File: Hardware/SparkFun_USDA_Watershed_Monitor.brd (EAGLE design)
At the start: 63.5 x 63.5 mm, 194 parts, among them J10 QWIIC_RIGHT_ANGLE, J3 QWIIC_RIGHT_ANGLE, J4 U.FL, J5 RJ45, J7 RJ45, J9 RJ45, Q1 20V/4.2A/52mΩ/1.4W, Q2 20V/0.2A/8MHz/1.2Ω/1Vth, Q3 20V/0.2A/8MHz/1.2Ω/1Vth, Q4 20V/0.2A/8MHz/1.2Ω/1Vth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

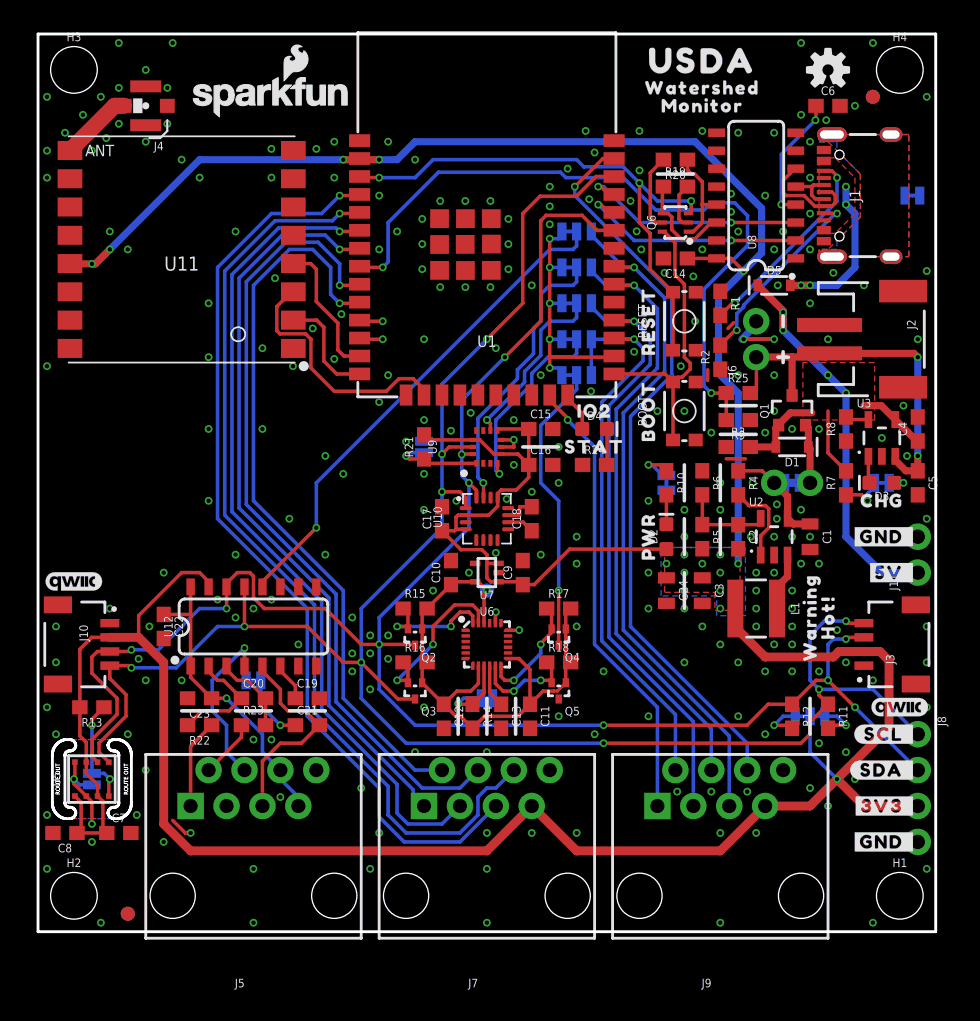
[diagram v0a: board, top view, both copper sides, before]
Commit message: Connect RFM95W pins
Somebody forgot to connect them...
Connect ESP32's IO5 and IO15 (both internally pulled high) to RFM's RESET and CS respectively
Connect ESP32's IO26 and IO27 to RFM's IO1 and IO0 respectively (IO2 not needed for LoRa)
ESP32's IO15, IO26, and IO27 are no longer broken out to RJ45 or headers
Add pullup resistor to ESP_EN
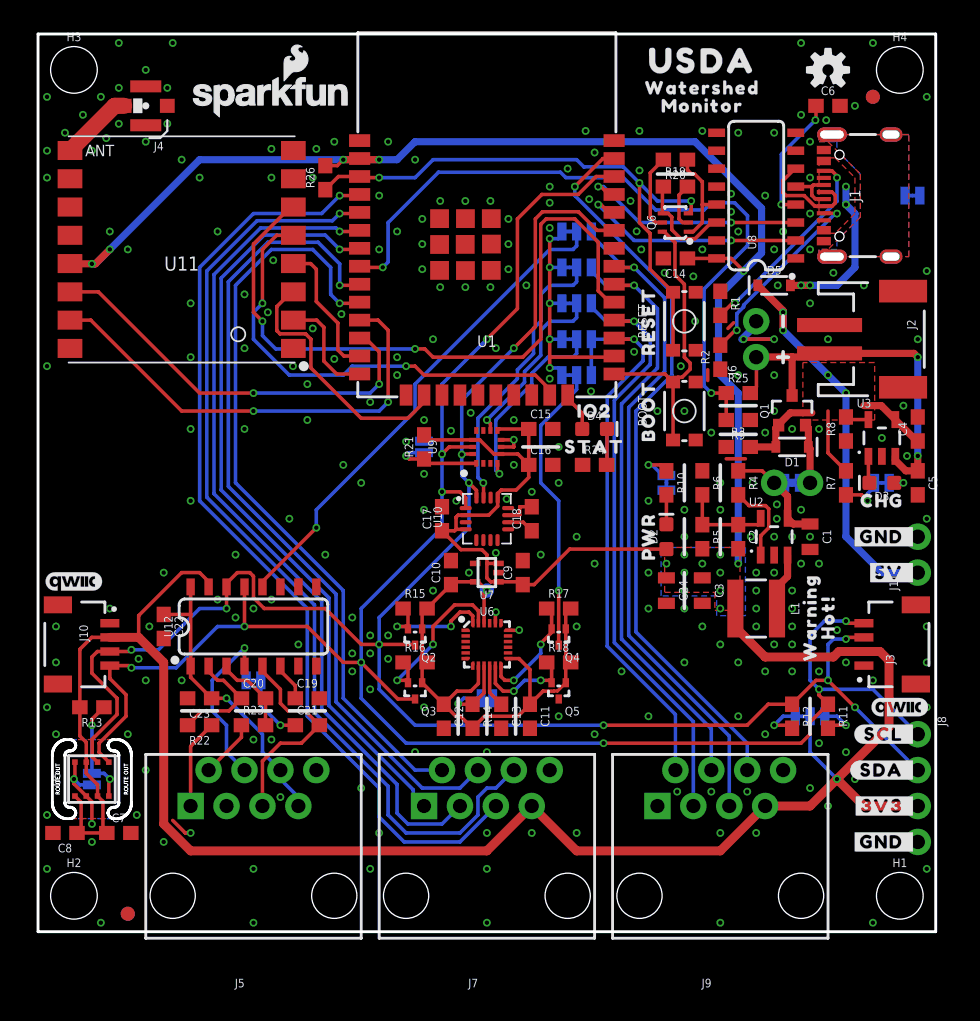
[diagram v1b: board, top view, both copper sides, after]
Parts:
- removed U$55: (no value), output:IO150
- added R26: 100k, SparkFun-Resistors:0603
- added U$49: (no value), output:NC0
- moved U$54 57.0 mm to (29.8, 3.05)
- moved U$63 54.0 mm to (33.7, 3.05)
- moved U$64 53.7 mm to (29.8, 4.57)
- moved U$61 53.3 mm to (33.7, 4.57)
- moved U$52 53.0 mm to (29.8, 6.10)
- moved U$62 49.0 mm to (33.7, 6.10)
- moved U$32 37.9 mm to (50.2, 18.8)
- moved U$33 37.9 mm to (46.4, 18.8)
- moved U$34 37.9 mm to (50.2, 17.3)
- moved U$35 37.9 mm to (46.4, 17.3)
- moved U$36 37.9 mm to (50.2, 15.7)
- moved U$37 37.9 mm to (46.4, 15.7)
- moved U$38 37.9 mm to (50.2, 14.2)
- moved U$39 37.9 mm to (46.4, 14.2)
- moved U$45 37.9 mm to (48.3, 20.3)
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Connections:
- removed net ESP_IO15: J9.1, U1.23
- removed net ESP_IO26: U1.11
- removed net ESP_IO27: U1.12
- removed net ESP_IO5: U1.29
- removed net IO26: U11.NSS
- removed net IO27: U11.DIO2
- removed net IO32: U11.DIO1
- removed net IO33: U11.DIO0
- new net !RFM_CS!: U1.23, U11.NSS
- new net RFM_IO0: U1.12, U11.DIO0
- new net RFM_IO1: U1.11, U11.DIO1
- net !RFM_RST!: now also U1.29
- net 3.3V: now also R26.2
- net ESP_EN: now also R26.1
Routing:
- net !RFM_RST!: track 0.00 -> 49.4 mm, vias 0 -> 2
- net RFM_IO1: track 0.00 -> 32.8 mm, vias 0 -> 2
- net !RFM_CS!: track 0.00 -> 32.6 mm, vias 0 -> 2
- net ESP_IO15: track 32.2 -> 0.00 mm, vias 1 -> 0
- net RFM_IO0: track 0.00 -> 29.2 mm, vias 0 -> 2
- net ESP_EN: track 39.0 -> 41.8 mm
- net ESP_IO33: track 56.8 -> 58.6 mm
- net ESP_I36: track 65.8 -> 67.6 mm
- net ESP_I34: track 58.8 -> 60.6 mm
- net ESP_IO25: track 52.2 -> 54.0 mm
- net ESP_I35: track 53.0 -> 54.8 mm
- net ESP_I39: track 66.5 -> 68.3 mm
- net ESP_IO27: track 1.67 -> 0.00 mm, vias 1 -> 0
- net ESP_IO26: track 1.67 -> 0.00 mm, vias 1 -> 0
- net 3.3V: track 267.7 -> 269.1 mm
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
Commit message: Design review updates
Remove 3V3_EN and ICM's FSYNC nets (won't be used)
Add diode to NAU_INT (chip doesn't do open-drain)
Clarify interrupts needing to be open-drain, active high
Fix ICM interrupt level shifter output to be high-Z when input is low (or high-Z), and drive high when input is high
Add version number to copper
Add silk labels to RJ45s, and dashed lines connecting pinout to color code
Add IMU axis albels to silk
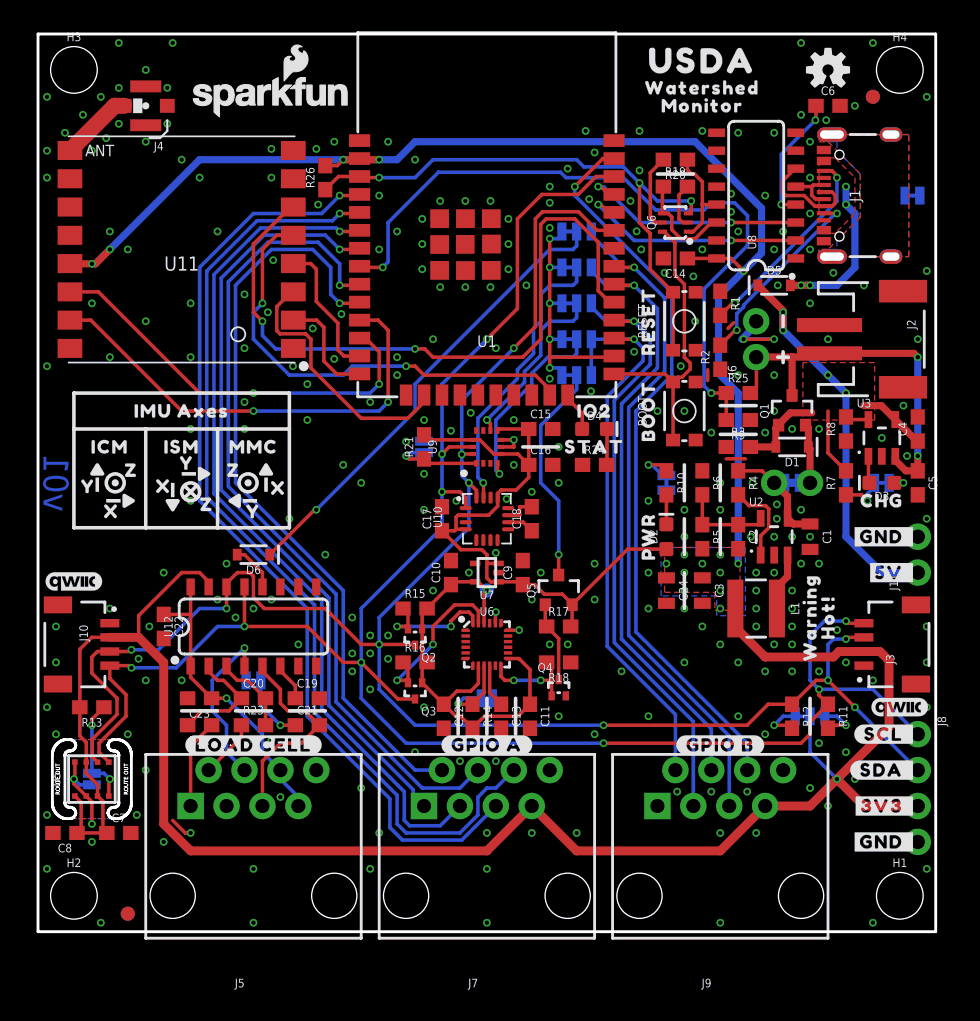
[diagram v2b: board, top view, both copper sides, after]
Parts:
- added D6: 3A/10V/280mV, SparkFun-DiscreteSemi:SOD-323
- added U$100, U$104, U$107, U$88, U$91, U$94: (no value), output:X0
- added U$101, U$113: (no value), output:IMU_AXES0
- added U$102, U$105, U$108, U$89, U$92, U$95: (no value), output:Y0
- added U$103, U$106, U$109, U$90, U$93, U$96: (no value), output:Z0
- added U$110, U$97: (no value), output:ICM0
- added U$111, U$98: (no value), output:ISM0
- added U$112, U$99: (no value), output:MMC0
- added U$50, U$55: (no value), output:#LOAD_CELL#0
- added U$51, U$86: (no value), output:#GPIO_A#0
- added U$53, U$87: (no value), output:#GPIO_B#0
- Q5: value 20V/0.2A/8MHz/1.2Ω/1Vth -> 20V/4.2A/52mΩ/1.4W; device SparkFun-DiscreteSemi:SOT-416FL -> SparkFun-DiscreteSemi:SOT23-3
- R17, R18: value 2.2k -> 100k
- moved Q5 7.62 mm to (36.8, 24.1), turned to 0 degrees
- moved Q4 2.54 mm to (36.8, 17.8), turned to 0 degrees
- moved R17 1.27 mm to (36.8, 21.6)
- moved U$12 0.38 mm to (17.1, 5.71)
- moved U$40 0.38 mm to (13.3, 5.71)
- moved U$41 0.38 mm to (17.1, 2.67)
- moved U$42 0.38 mm to (13.3, 2.67)
- moved U$43 0.38 mm to (17.1, 4.19)
- moved U$44 0.38 mm to (13.3, 4.19)
- moved U$49 0.38 mm to (50.2, 5.71)
- moved U$52 0.38 mm to (29.8, 5.71)
- moved U$54 0.38 mm to (29.8, 2.67)
- moved U$57 0.38 mm to (46.4, 5.71)
- moved U$58 0.38 mm to (50.2, 4.19)
- moved U$59 0.38 mm to (46.4, 2.67)
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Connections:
- removed net ICM_FSYNC: Q5.3
- removed net ICM_FSYNC_1V8: Q5.2, R18.1, U6.11
- new net N$29: D6.A, U12.12
- new net N$30: Q4.3, Q5.1, R17.1
- net 1.8V: no longer Q4.1, Q5.1, R17.2, R18.2
- net 3.3V: now also Q5.2, R17.2
- net GND: now also Q4.2, R18.1
- net ICM_INT: now also Q5.3; no longer Q4.3
- net ICM_INT_1V8: now also Q4.1, R18.2; no longer Q4.2, R17.1
- net NAU_INT: now also D6.C; no longer U12.12
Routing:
- net 1.8V: track 40.4 -> 31.6 mm
- net ICM_FSYNC_1V8: track 7.43 -> 0.00 mm, vias 2 -> 0
- net N$30: track 0.00 -> 5.69 mm
- net ICM_INT: track 20.7 -> 15.7 mm
- net N$29: track 0.00 -> 3.32 mm
- net 3.3V: track 269.1 -> 271.9 mm
- net NAU_INT: track 35.3 -> 32.9 mm
- net ICM_INT_1V8: track 8.07 -> 6.92 mm
- net GND: vias 264 -> 271
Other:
- board text added: "v01"

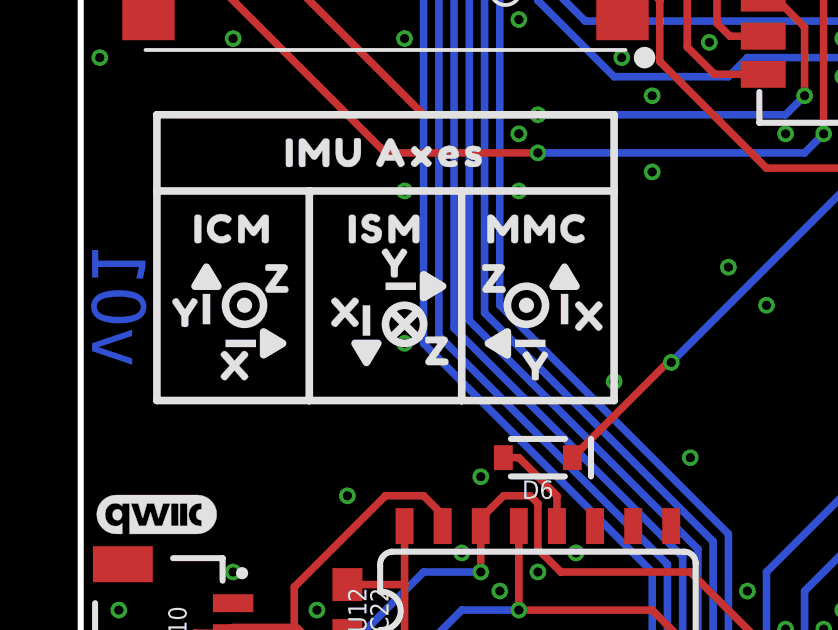
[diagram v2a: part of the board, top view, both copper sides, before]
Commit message: Checklist updates
Add measures or PTH pads
Copy SFE logo and board name silk on back side
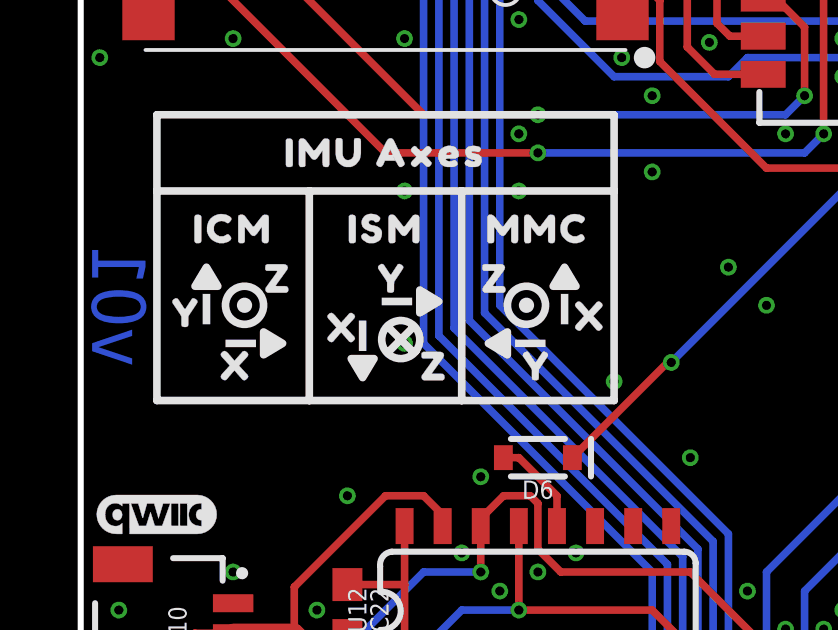
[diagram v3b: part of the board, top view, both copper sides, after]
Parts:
- added LOGO5: SFE_LOGO_NAME_FLAME.1_INCH, SparkFun-Aesthetics:SFE_LOGO_NAME_FLAME_.1
- added U$114: (no value), output:USDA0
- added U$115: (no value), output:WATERSHED0
- added U$116: (no value), output:MONITOR0
- moved U$104 0.52 mm to (8.64, 31.0)
- moved U$106 0.52 mm to (11.7, 29.7)
- moved U$91 0.52 mm to (8.76, 31.0)
- moved U$93 0.52 mm to (11.8, 29.7)
- moved U$92 0.52 mm to (10.4, 32.6)
- moved U$105 0.52 mm to (10.3, 32.6)
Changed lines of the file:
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@@
 <dimension x1="0" y1="0" x2="0" y2="60.96" x3="-20.32" y3="30.48" textsize="1.778" textratio="15" layer="47" unit="inch"/>
 <dimension x1="0" y1="0" x2="0" y2="63.5" x3="-24.13" y3="31.75" textsize="1.778" textratio="15" layer="47" unit="inch"/>
-<dimension x1="63.5" y1="0" x2="63.5" y2="20.32" x3="67.31" y3="10.16" textsize="1.778" textratio="15" layer="47" unit="inch"/>
-<dimension x1="63.5" y1="0" x2="63.5" y2="41.91" x3="71.12" y3="20.955" textsize="1.778" textratio="15" layer="47" unit="inch"/>
-<dimension x1="63.5" y1="0" x2="63.5" y2="52.07" x3="74.93" y3="26.035" textsize="1.778" textratio="15" layer="47" unit="inch"/>
+<dimension x1="63.5" y1="0" x2="63.5" y2="20.32" x3="74.93" y3="10.16" textsize="1.778" textratio="15" layer="47" unit="inch"/>
+<dimension x1="63.5" y1="0" x2="63.5" y2="41.91" x3="86.36" y3="20.955" textsize="1.778" textratio="15" layer="47" unit="inch"/>
+<dimension x1="63.5" y1="0" x2="63.5" y2="52.07" x3="90.17" y3="26.035" textsize="1.778" textratio="15" layer="47" unit="inch"/>
 <dimension x1="0" y1="63.5" x2="7.62" y2="63.5" x3="3.81" y3="64.77" textsize="1.778" textratio="15" layer="47" unit="inch"/>
 <polygon width="0.1016" layer="22">
@@
 <vertex x="4.572" y="32.385"/>
 </polygon>
-<circle x="10.795" y="31.115" radius="0.635" width="0.254" layer="21"/>
-<wire x1="9.525" y1="31.75" x2="9.525" y2="29.845" width="0.254" layer="21" style="shortdash"/>
-<wire x1="10.16" y1="32.385" x2="12.065" y2="32.385" width="0.254" layer="21" style="shortdash"/>
+<circle x="10.668" y="30.607" radius="0.635" width="0.254" layer="21"/>
+<wire x1="9.398" y1="31.242" x2="9.398" y2="29.337" width="0.254" layer="21" style="shortdash"/>
+<wire x1="10.033" y1="31.877" x2="11.938" y2="31.877" width="0.254" layer="21" style="shortdash"/>
 <polygon width="0.254" layer="21">
-<vertex x="9.525" y="29.845"/>
-<vertex x="9.906" y="30.48"/>
-<vertex x="9.144" y="30.48"/>
+<vertex x="9.398" y="29.337"/>
+<vertex x="9.779" y="29.972"/>
+<vertex x="9.017" y="29.972"/>
 </polygon>
 <polygon width="0.254" layer="21">
-<vertex x="12.065" y="32.385"/>
-<vertex x="11.43" y="32.766"/>
-<vertex x="11.43" y="32.004"/>
+<vertex x="11.938" y="31.877"/>
+<vertex x="11.303" y="32.258"/>
+<vertex x="11.303" y="31.496"/>
 </polygon>
 <circle x="14.859" y="31.75" radius="0.127" width="0.254" layer="21"/>
@@
 <wire x1="7.62" y1="35.56" x2="7.62" y2="28.575" width="0.254" layer="21"/>
 <wire x1="12.7" y1="35.56" x2="12.7" y2="28.575" width="0.254" layer="21"/>
-<wire x1="10.414" y1="31.496" x2="11.176" y2="30.734" width="0.254" layer="21"/>
-<wire x1="11.176" y1="30.734" x2="11.303" y2="30.734" width="0.254" layer="21"/>
-<wire x1="10.414" y1="30.734" x2="11.176" y2="31.496" width="0.254" layer="21"/>
+<wire x1="10.287" y1="30.988" x2="11.049" y2="30.226" width="0.254" layer="21"/>
+<wire x1="11.049" y1="30.226" x2="11.176" y2="30.226" width="0.254" layer="21"/>
+<wire x1="10.287" y1="30.226" x2="11.049" y2="30.988" width="0.254" layer="21"/>
 <circle x="5.461" y="31.75" radius="0.635" width="0.254" layer="22"/>
 <wire x1="4.826" y1="30.48" x2="6.731" y2="30.48" width="0.254" layer="22" style="shortdash"/>
@@
 <vertex x="3.81" y="32.385"/>
 </polygon>
-<circle x="10.795" y="31.115" radius="0.635" width="0.254" layer="22"/>
-<wire x1="9.525" y1="31.75" x2="9.525" y2="29.845" width="0.254" layer="22" style="shortdash"/>
-<wire x1="10.16" y1="32.385" x2="12.065" y2="32.385" width="0.254" layer="22" style="shortdash"/>
+<circle x="10.668" y="30.607" radius="0.635" width="0.254" layer="22"/>
+<wire x1="9.398" y1="31.242" x2="9.398" y2="29.337" width="0.254" layer="22" style="shortdash"/>
+<wire x1="10.033" y1="31.877" x2="11.938" y2="31.877" width="0.254" layer="22" style="shortdash"/>
 <polygon width="0.254" layer="22">
-<vertex x="9.525" y="29.845"/>
-<vertex x="9.144" y="30.48"/>
-<vertex x="9.906" y="30.48"/>
+<vertex x="9.398" y="29.337"/>
+<vertex x="9.017" y="29.972"/>
+<vertex x="9.779" y="29.972"/>
 </polygon>
 <polygon width="0.254" layer="22">
-<vertex x="12.065" y="32.385"/>
-<vertex x="11.43" y="32.004"/>
-<vertex x="11.43" y="32.766"/>
+<vertex x="11.938" y="31.877"/>
+<vertex x="11.303" y="31.496"/>
+<vertex x="11.303" y="32.258"/>
 </polygon>
 <circle x="14.859" y="31.75" radius="0.635" width="0.254" layer="22"/>
@@
 <wire x1="12.7" y1="35.56" x2="12.7" y2="28.575" width="0.254" layer="22"/>
 <wire x1="7.62" y1="35.56" x2="7.62" y2="28.575" width="0.254" layer="22"/>
-<circle x="10.795" y="31.115" radius="0.127" width="0.254" layer="22"/>
+<circle x="10.668" y="30.607" radius="0.127" width="0.254" layer="22"/>
 <wire x1="15.24" y1="32.131" x2="14.478" y2="31.369" width="0.254" layer="22"/>
 <wire x1="15.24" y1="31.369" x2="14.478" y2="32.131" width="0.254" layer="22"/>
 <wire x1="5.842" y1="32.131" x2="5.08" y2="31.369" width="0.254" layer="22"/>
 <wire x1="5.842" y1="31.369" x2="5.08" y2="32.131" width="0.254" layer="22"/>
+<dimension x1="63.5" y1="0" x2="63.5" y2="6.35" x3="67.31" y3="3.175" textsize="1.778" textratio="15" layer="47" unit="inch"/>
+<dimension x1="63.5" y1="0" x2="63.5" y2="13.97" x3="71.12" y3="6.985" textsize="1.778" textratio="15" layer="47" unit="inch"/>
+<dimension x1="63.5" y1="0" x2="63.5" y2="25.4" x3="78.74" y3="12.7" textsize="1.778" textratio="15" layer="47" unit="inch"/>
+<dimension x1="63.5" y1="0" x2="63.5" y2="27.94" x3="82.55" y3="13.97" textsize="1.778" textratio="15" layer="47" unit="inch"/>
 </plain>
 <attributes>
@@
 <element name="U$89" library="output" package="Y0" value="" x="3.556" y="31.496" smashed="yes"/>
 <element name="U$90" library="output" package="Z0" value="" x="6.604" y="32.639" smashed="yes"/>
-<element name="U$91" library="output" package="X0" value="" x="8.89" y="31.496" smashed="yes"/>
-<element name="U$92" library="output" package="Y0" value="" x="10.541" y="33.147" smashed="yes"/>
-<element name="U$93" library="output" package="Z0" value="" x="11.938" y="30.226" smashed="yes"/>
+<element name="U$91" library="output" package="X0" value="" x="8.763" y="30.988" smashed="yes"/>
+<element name="U$92" library="output" package="Y0" value="" x="10.414" y="32.639" smashed="yes"/>
+<element name="U$93" library="output" package="Z0" value="" x="11.811" y="29.718" smashed="yes"/>
 <element name="U$94" library="output" package="X0" value="" x="17.018" y="31.369" smashed="yes"/>
 <element name="U$95" library="output" package="Y0" value="" x="15.24" y="29.718" smashed="yes"/>
@@
 <element name="U$102" library="output" package="Y0" value="" x="3.429" y="31.496" smashed="yes" rot="MR0"/>
 <element name="U$103" library="output" package="Z0" value="" x="6.477" y="32.639" smashed="yes" rot="MR0"/>
-<element name="U$104" library="output" package="X0" value="" x="8.763" y="31.496" smashed="yes" rot="MR0"/>
-<element name="U$105" library="output" package="Y0" value="" x="10.414" y="33.147" smashed="yes" rot="MR0"/>
-<element name="U$106" library="output" package="Z0" value="" x="11.811" y="30.226" smashed="yes" rot="MR0"/>
+<element name="U$104" library="output" package="X0" value="" x="8.636" y="30.988" smashed="yes" rot="MR0"/>
+<element name="U$105" library="output" package="Y0" value="" x="10.287" y="32.639" smashed="yes" rot="MR0"/>
+<element name="U$106" library="output" package="Z0" value="" x="11.684" y="29.718" smashed="yes" rot="MR0"/>
 <element name="U$107" library="output" package="X0" value="" x="16.891" y="31.369" smashed="yes" rot="MR0"/>
 <element name="U$108" library="output" package="Y0" value="" x="15.113" y="29.718" smashed="yes" rot="MR0"/>
@@
 <element name="U$112" library="output" package="MMC0" value="" x="15.24" y="34.29" smashed="yes" rot="MR0"/>
 <element name="U$113" library="output" package="IMU_AXES0" value="" x="10.16" y="36.83" smashed="yes" rot="MR0"/>
+<element name="LOGO5" library="SparkFun-Aesthetics" package="SFE_LOGO_NAME_FLAME_.1" value="SFE_LOGO_NAME_FLAME.1_INCH" x="46.99" y="59.055" smashed="yes" rot="MR0"/>
+<element name="U$114" library="output" package="USDA0" value="" x="16.51" y="61.595" smashed="yes" rot="MR0"/>
+<element name="U$115" library="output" package="WATERSHED0" value="" x="16.51" y="59.69" smashed="yes" rot="MR0"/>
+<element name="U$116" library="output" package="MONITOR0" value="" x="16.51" y="58.42" smashed="yes" rot="MR0"/>
 </elements>
 <signals>
